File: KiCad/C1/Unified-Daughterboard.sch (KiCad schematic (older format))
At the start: 8 parts, among them J1 HRO-TYPE-C-31-M-12, J2 Conn_01x04

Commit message: Organized schematic
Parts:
- J1: symbol Type-C:HRO-TYPE-C-31-M-12 -> Unified-Daughterboard-rescue:HRO-TYPE-C-31-M-12-Type-C
- J2: value Conn_01x04 -> JST-SR-4
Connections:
- net at J1.10 (CC2): now also R2.1; no longer R1.1
- net at J1.4 (CC1): now also R1.1; no longer R2.1
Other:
- moved on the sheet: J1, J2, MH1, MH2, MH3, MH4, R1, R2

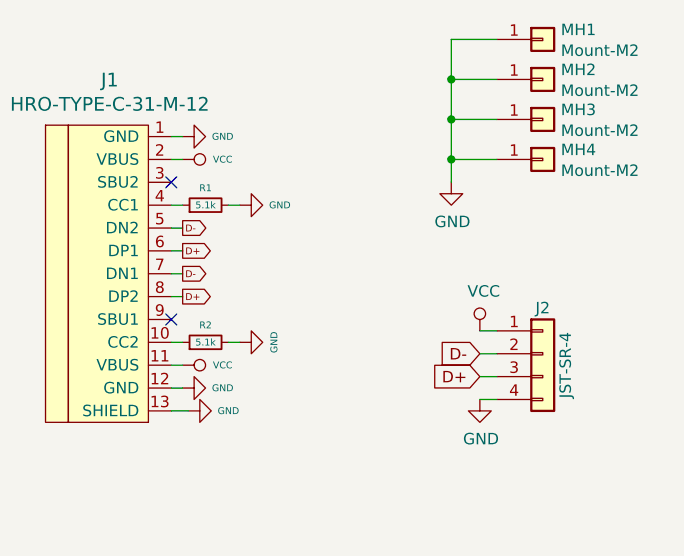
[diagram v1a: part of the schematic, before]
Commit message: Improved grounding and shielding
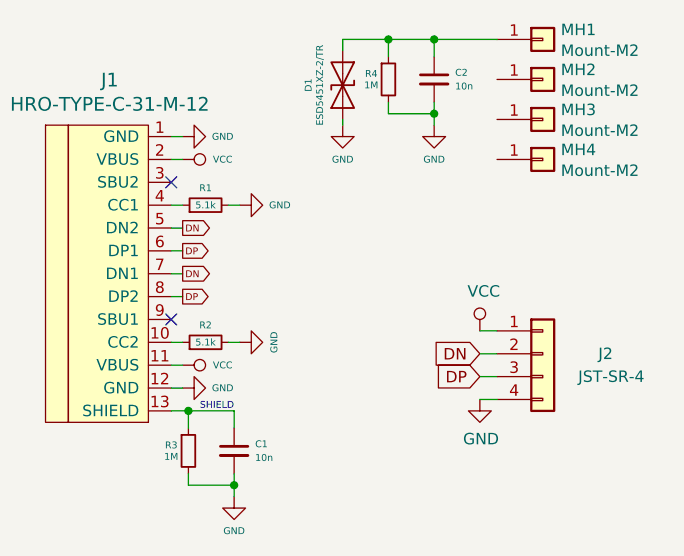
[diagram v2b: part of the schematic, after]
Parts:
- added C1, C2: 10n, Capacitor_SMD:C_0603_1608Metric, symbol Device:C_Small
- added D1: ESD5451XZ-2/TR, Diode_SMD:D_0603_1608Metric, symbol Device:D_TVS
- added R3, R4: 1M, Resistor_SMD:R_0603_1608Metric, symbol Device:R_Small
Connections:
- net GND: now also C1.2, C2.2, D1.1 (A1), R3.2, R4.2; no longer J1.13 (SHIELD), MH1.1 (Pin_1), MH2.1 (Pin_1), MH3.1 (Pin_1), MH4.1 (Pin_1)
- net D+ renamed DP
- net D- renamed DN
- new net: C1.1, J1.13 (SHIELD), R3.1
- new net: C2.1, D1.2 (A2), MH1.1 (Pin_1), R4.1
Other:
- note added: "SHIELD\n"
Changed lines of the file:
@@
 U 1 1 5C91AFCB
 P 6400 4175
-F 0 "J2" H 6400 4375 50  0000 C CNN
-F 1 "JST-SR-4" V 6500 4125 50  0000 C CNN
+F 0 "J2" H 6675 4175 50  0000 C CNN
+F 1 "JST-SR-4" H 6700 4075 50  0000 C CNN
 F 2 "random-keyboard-parts:JST-SR-4" H 6400 4175 50  0001 C CNN
 F 3 "~" H 6400 4175 50  0001 C CNN
@@
 $EndComp
 Text GLabel 6125 4175 0    50   Input ~ 0
-D-
+DN
 Text GLabel 6125 4275 0    50   Input ~ 0
-D+
+DP
 $Comp
 L Connector_Generic:Conn_01x01 MH1
@@
 $EndComp
 $Comp
-L power:GND #PWR0105
-U 1 1 5C91FF24
-P 6000 3425
-F 0 "#PWR0105" H 6000 3175 50  0001 C CNN
-F 1 "GND" H 6005 3252 50  0000 C CNN
-F 2 "" H 6000 3425 50  0001 C CNN
-F 3 "" H 6000 3425 50  0001 C CNN
-	1    6000 3425
-	1    0    0    -1
-$EndComp
-Wire Wire Line
-	6200 2800 6000 2800
-Wire Wire Line
-	6000 3425 6000 3325
-Wire Wire Line
-	6200 2975 6000 2975
-Connection ~ 6000 2975
-Wire Wire Line
-	6000 2975 6000 2800
-Wire Wire Line
-	6000 3150 6200 3150
-Connection ~ 6000 3150
-Wire Wire Line
-	6000 3150 6000 2975
-Wire Wire Line
-	6200 3325 6000 3325
-Connection ~ 6000 3325
-Wire Wire Line
-	6000 3325 6000 3150
-$Comp
-L power:GND #PWR?
+L power:GND #PWR0102
 U 1 1 5E156061
 P 4825 3225
-F 0 "#PWR?" H 4825 2975 50  0001 C CNN
+F 0 "#PWR0102" H 4825 2975 50  0001 C CNN
 F 1 "GND" V 4825 3050 30  0000 C CNN
 F 2 "" H 4825 3225 50  0001 C CNN
@@
 $EndComp
 $Comp
-L power:GND #PWR?
+L power:GND #PWR0105
 U 1 1 5E15AA04
 P 5075 3525
-F 0 "#PWR?" H 5075 3275 50  0001 C CNN
+F 0 "#PWR0105" H 5075 3275 50  0001 C CNN
 F 1 "GND" V 5075 3350 30  0000 C CNN
 F 2 "" H 5075 3525 50  0001 C CNN
@@
 	4825 4125 4775 4125
 $Comp
-L power:GND #PWR?
+L power:GND #PWR0106
 U 1 1 5E15E3A0
 P 5075 4125
-F 0 "#PWR?" H 5075 3875 50  0001 C CNN
+F 0 "#PWR0106" H 5075 3875 50  0001 C CNN
 F 1 "GND" H 5075 3975 30  0000 C CNN
 F 2 "" H 5075 4125 50  0001 C CNN
@@
 	5075 4125 5025 4125
 $Comp
-L power:GND #PWR?
+L power:GND #PWR0107
 U 1 1 5E15EFD8
 P 4825 4325
-F 0 "#PWR?" H 4825 4075 50  0001 C CNN
+F 0 "#PWR0107" H 4825 4075 50  0001 C CNN
 F 1 "GND" V 4825 4150 30  0000 C CNN
 F 2 "" H 4825 4325 50  0001 C CNN
 F 3 "" H 4825 4325 50  0001 C CNN
 	1    4825 4325
-	0    -1   -1   0
+	0    -1   1    0
 $EndComp
 Wire Wire Line
 	4775 4325 4825 4325
 $Comp
-L power:VCC #PWR?
+L power:VCC #PWR0108
 U 1 1 5E160B0A
 P 4825 4225
-F 0 "#PWR?" H 4825 4075 50  0001 C CNN
+F 0 "#PWR0108" H 4825 4075 50  0001 C CNN
 F 1 "VCC" V 4825 4400 30  0000 C CNN
 F 2 "" H 4825 4225 50  0001 C CNN
@@
 	4825 4225 4775 4225
 Text GLabel 4825 3925 2    30   Output ~ 0
-D+
+DP
 Text GLabel 4825 3725 2    30   Output ~ 0
-D+
+DP
 Text GLabel 4825 3825 2    30   Output ~ 0
-D-
+DN
 Text GLabel 4825 3625 2    30   Output ~ 0
-D-
+DN
 Wire Wire Line
 	4775 3625 4825 3625
@@
 Wire Wire Line
 	4775 3925 4825 3925
-$Comp
-L power:GND #PWR?
-U 1 1 5E164F86
-P 4850 4425
-F 0 "#PWR?" H 4850 4175 50  0001 C CNN
-F 1 "GND" V 4850 4250 30  0000 C CNN
-F 2 "" H 4850 4425 50  0001 C CNN
-F 3 "" H 4850 4425 50  0001 C CNN
-	1    4850 4425
-	0    -1   -1   0
-$EndComp
 Wire Wire Line
 	4775 4425 4850 4425
 Wire Wire Line
 	6200 4175 6125 4175
+$Comp
+L Device:R_Small R3
+U 1 1 5E17225D
+P 4850 4600
+F 0 "R3" H 4775 4625 30  0000 C CNN
+F 1 "1M" H 4775 4575 30  0000 C CNN
+F 2 "Resistor_SMD:R_0603_1608Metric" H 4850 4600 50  0001 C CNN
+F 3 "~" H 4850 4600 50  0001 C CNN
+	1    4850 4600
+	1    0    0    -1
+$EndComp
+$Comp
+L Device:C_Small C1
+U 1 1 5E172A5B
+P 5050 4600
+F 0 "C1" H 5142 4630 30  0000 L CNN
+F 1 "10n" H 5142 4570 30  0000 L CNN
+F 2 "Capacitor_SMD:C_0603_1608Metric" H 5050 4600 50  0001 C CNN
+F 3 "~" H 5050 4600 50  0001 C CNN
+	1    5050 4600
+	1    0    0    -1
+$EndComp
+Wire Wire Line
+	4850 4425 5050 4425
+Wire Wire Line
+	5050 4425 5050 4500
+Wire Wire Line
+	5050 4750 4850 4750
+Wire Wire Line
+	4850 4750 4850 4700
+Wire Wire Line
+	4850 4500 4850 4425
+Wire Wire Line
+	5050 4700 5050 4750
+Connection ~ 4850 4425
+$Comp
+L power:GND #PWR0109
+U 1 1 5E173B1D
+P 5050 4800
+F 0 "#PWR0109" H 5050 4550 50  0001 C CNN
+F 1 "GND" H 5050 4650 30  0000 C CNN
+F 2 "" H 5050 4800 50  0001 C CNN
+F 3 "" H 5050 4800 50  0001 C CNN
+	1    5050 4800
+	1    0    0    -1
+$EndComp
+Wire Wire Line
+	5050 4800 5050 4750
+Connection ~ 5050 4750
+Text Notes 4900 4425 0    30   ~ 0
+SHIELD\n
+$Comp
+L Device:R_Small R4
+U 1 1 5E17CC01
+P 5725 2975
+F 0 "R4" H 5650 3000 30  0000 C CNN
+F 1 "1M" H 5650 2950 30  0000 C CNN
+F 2 "Resistor_SMD:R_0603_1608Metric" H 5725 2975 50  0001 C CNN
+F 3 "~" H 5725 2975 50  0001 C CNN
+	1    5725 2975
+	1    0    0    -1
+$EndComp
+$Comp
+L Device:C_Small C2
+U 1 1 5E17CC07
+P 5925 2975
+F 0 "C2" H 6017 3005 30  0000 L CNN
+F 1 "10n" H 6017 2945 30  0000 L CNN
+F 2 "Capacitor_SMD:C_0603_1608Metric" H 5925 2975 50  0001 C CNN
+F 3 "~" H 5925 2975 50  0001 C CNN
+	1    5925 2975
+	1    0    0    -1
+$EndComp
+Wire Wire Line
+	5725 2800 5925 2800
+Wire Wire Line
+	5925 2800 5925 2875
+Wire Wire Line
+	5925 3125 5725 3125
+Wire Wire Line
+	5725 3125 5725 3075
+Wire Wire Line
+	5725 2875 5725 2800
+Wire Wire Line
+	5925 3075 5925 3125
+$Comp
+L power:GND #PWR0110
+U 1 1 5E17CC14
+P 5925 3175
+F 0 "#PWR0110" H 5925 2925 50  0001 C CNN
+F 1 "GND" H 5925 3025 30  0000 C CNN
+F 2 "" H 5925 3175 50  0001 C CNN
+F 3 "" H 5925 3175 50  0001 C CNN
+	1    5925 3175
+	1    0    0    -1
+$EndComp
+Connection ~ 5925 2800
+$Comp
+L Device:D_TVS D1
+U 1 1 5E18209E
+P 5525 3000
+F 0 "D1" H 5525 2850 30  0000 C CNN
+F 1 "ESD5451XZ-2/TR" H 5525 2900 30  0000 C CNN
+F 2 "Diode_SMD:D_0603_1608Metric" H 5525 3000 50  0001 C CNN
+F 3 "~" H 5525 3000 50  0001 C CNN
+F 4 "D0603" H 5525 3000 50  0001 C CNN "Package"
+	1    5525 3000
+	0    1    -1   0
+$EndComp
+Wire Wire Line
+	5925 3175 5925 3125
+Connection ~ 5925 3125
+$Comp
+L power:GND #PWR0111
+U 1 1 5E18A821
+P 5525 3175
+F 0 "#PWR0111" H 5525 2925 50  0001 C CNN
+F 1 "GND" H 5525 3025 30  0000 C CNN
+F 2 "" H 5525 3175 50  0001 C CNN
+F 3 "" H 5525 3175 50  0001 C CNN
+	1    5525 3175
+	1    0    0    -1
+$EndComp
+Wire Wire Line
+	5525 2800 5725 2800
+Wire Wire Line
+	5525 2850 5525 2800
+Connection ~ 5725 2800
+Wire Wire Line
+	5525 3175 5525 3150
+Wire Wire Line
+	5925 2800 6200 2800
 $EndSCHEMATC
